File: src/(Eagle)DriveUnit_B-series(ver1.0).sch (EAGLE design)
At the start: 55 parts, among them IC1 A3921, SW1 TVAF06-A020B-R, SW2 TVAF06-A020B-R, SW3 THAF01-NC-R, SW4 SS-12D00G3

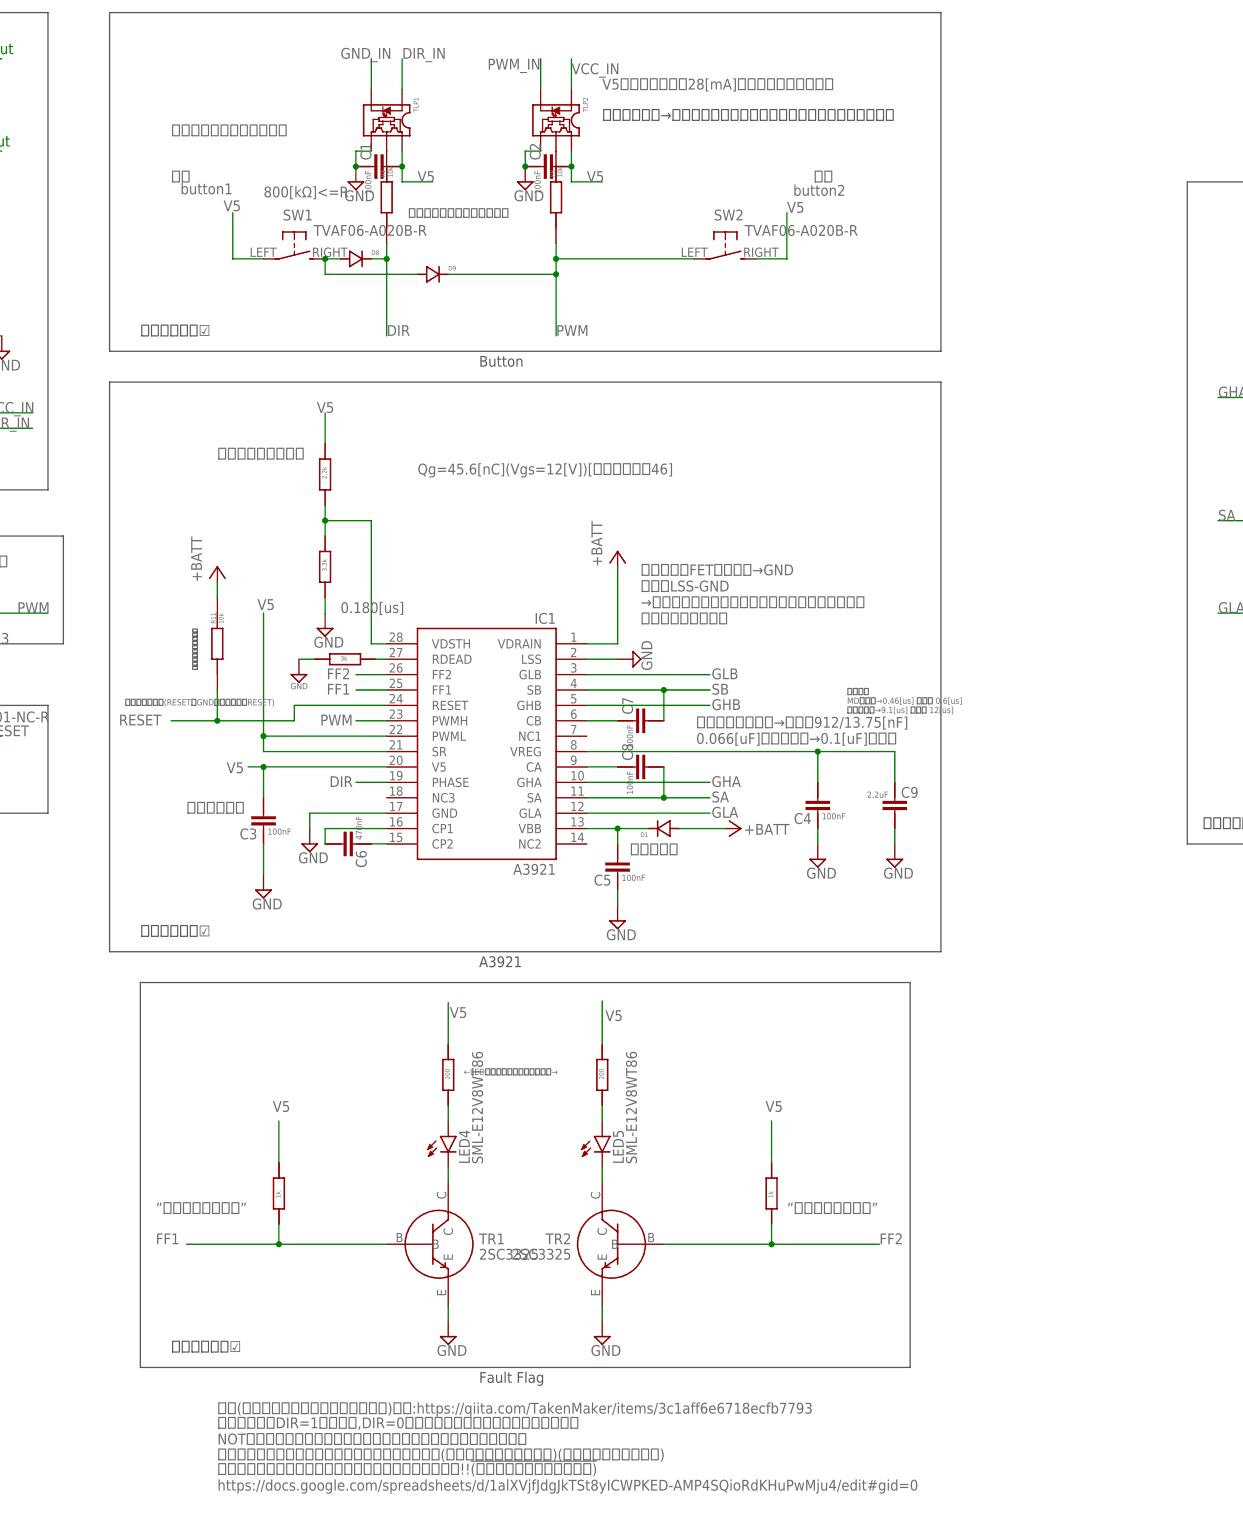
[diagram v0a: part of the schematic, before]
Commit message: [fix]入力周りなどの変更(ver1.0の問題点の修復)
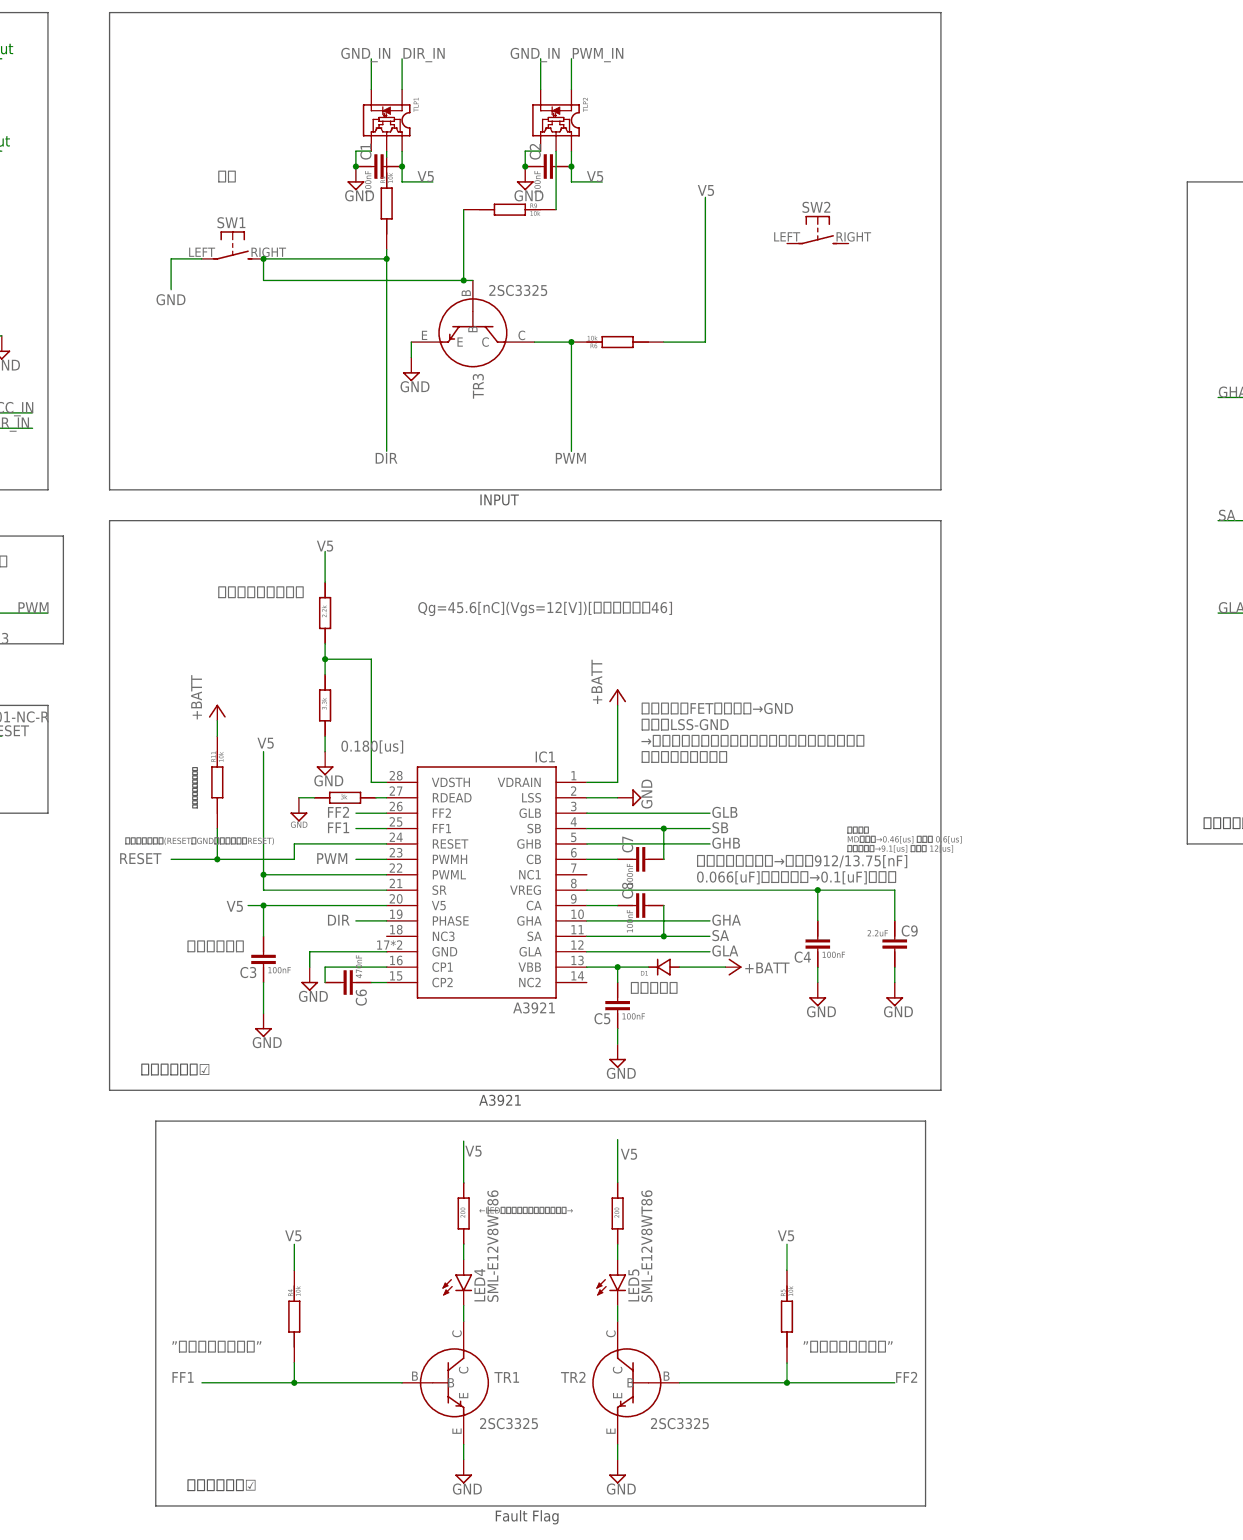
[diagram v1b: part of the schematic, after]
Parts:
- removed D8, D9: GS1010FL, GS1010FL:GS1010FL
- added R4: RG2012, RG2012:RG2012
- added TR3: 2SC3325, 2SC3325:2SC3325
- R5, R6: value RG2012-N-102-B-T5 -> RG2012; device RG2012-N-102-B-T5:RG2012-N-102-B-T5 -> RG2012:RG2012
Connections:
- removed net N$12: D8.A, D9.A, SW1.S
- net DIR: now also R9.LEFT, SW1.S, TR3.B; no longer D8.C
- net FF1: now also R4.LEFT; no longer R5.P$2
- net FF2: now also R5.LEFT; no longer R6.P$2
- net GND: now also SW1.P, TR3.E
- net GND_IN: now also TLP2.CATHODE
- net PWM: now also R6.RIGHT, TR3.C; no longer D9.C, R9.LEFT, SW2.P
- net PWM_IN: now also TLP2.ANODE; no longer TLP2.CATHODE
- net V5: now also R4.RIGHT, R5.RIGHT, R6.LEFT; no longer R5.P$1, R6.P$1, SW1.P, SW2.S
- net VCC_IN: no longer TLP2.ANODE
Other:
- note added: "INPUT"
- note removed: "800[kΩ]<=R"
- note removed: "Button"
- note removed: "DIR"
- note removed: "GHA"
- note removed: "GLA"
- note removed: "PWM"
- note removed: "V5の最大駆動電流28[mA]を超えないようにする"
- note removed: "button1"
- note removed: "button2"
- note removed: "この抵抗つけないと多分だめ"
- note removed: "パスコン、昇圧用コンデンサ、抵抗等は今は仮決め(適当なスルーホール部品)(後で消すのを忘れない)"
- note removed: "フォトカプラ→モタドラの駆動周波数に影響を与える可能性がある"
- note removed: "プルダウン抵抗の値は適当"
- note removed: "今の設計ではDIR=1の時正転,DIR=0の時逆転であり、野獣と逆になっている NOT回路をつければ解決可能だが部品点数が多くなり費用が高くなる"
- note removed: "作業する前にここにきてステータスをオンに変えるんだ!!!(やることも書いてあります) https://docs.google.com/spreadsheets/d/1alXVjfJdgJkTSt8yICWPKED-AMP4SQioRdKHuPwMju4/edit#gid=0"
- note removed: "参考(にしないほうがいいかもしれない)記事:https://qiita.com/TakenMaker/items/3c1aff6e6718ecfb7793"
- note removed: "逆転"
- moved on the sheet: C3, C4, C5, C6, C7, C8, C9, D1, IC1, LED4, LED5, R1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
